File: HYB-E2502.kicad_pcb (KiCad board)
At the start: 2 copper layers, 50 x 40 mm, 23 parts, among them J1 USB4105-GF-A, U1 CH340C, U2 IM920SL, U3 NCP1117ST33T3G

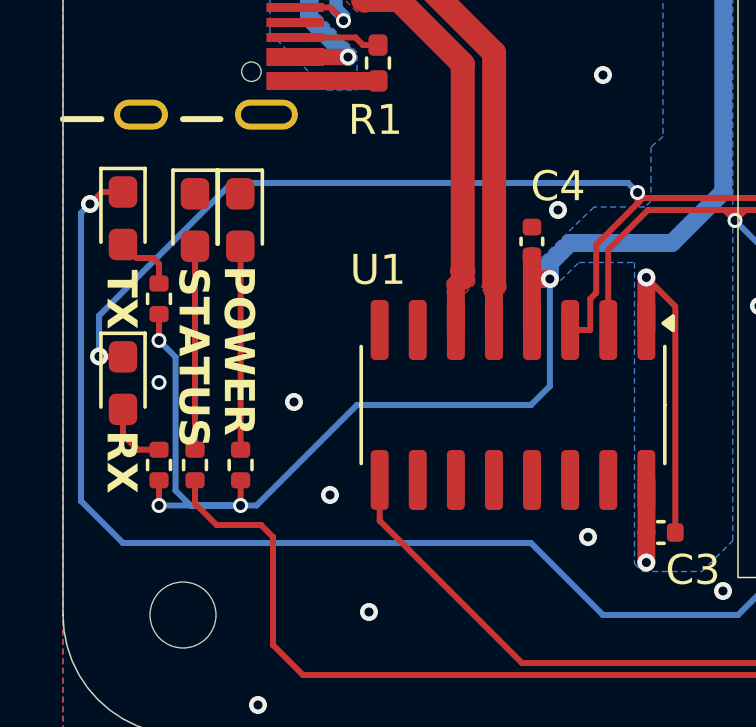
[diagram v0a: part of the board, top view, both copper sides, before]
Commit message: Edit/PCB
TX RX LEDの抵抗の位置を変更
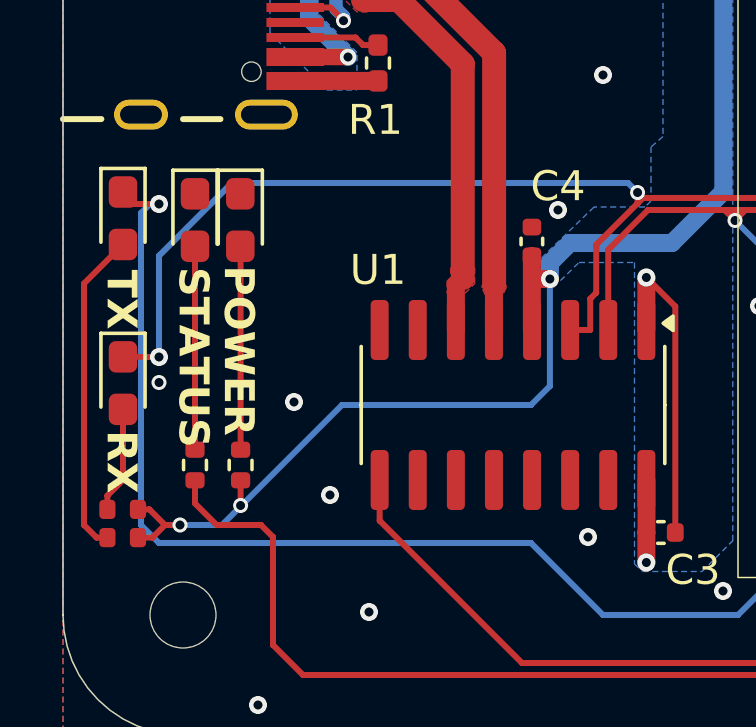
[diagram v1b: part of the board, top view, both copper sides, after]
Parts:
- moved R6 8.05 mm to (102.0, 93.4), turned to 180 degrees
- moved R5 1.91 mm to (102.0, 92.5), turned to 180 degrees
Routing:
- net Net-(D4-A): track 2.12 -> 10.8 mm
- net +3.3V: track 90.4 -> 83.3 mm, vias 6 -> 5
- net Net-(D3-A): track 2.26 -> 3.55 mm
- net Net-(D4-K): track 80.7 -> 79.6 mm
- net Net-(D3-K): track 59.7 -> 59.2 mm

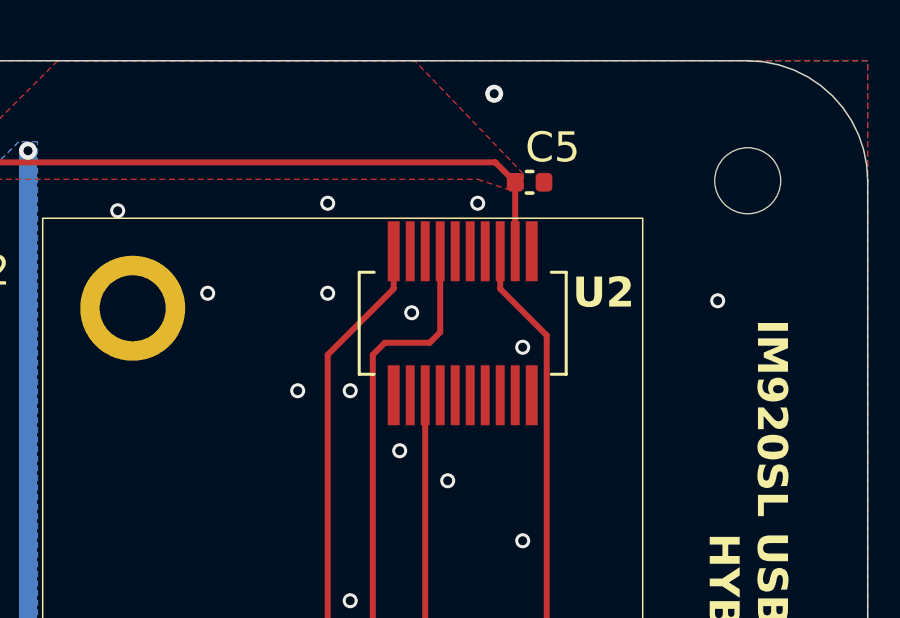
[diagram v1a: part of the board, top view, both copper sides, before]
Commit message: 配線修正
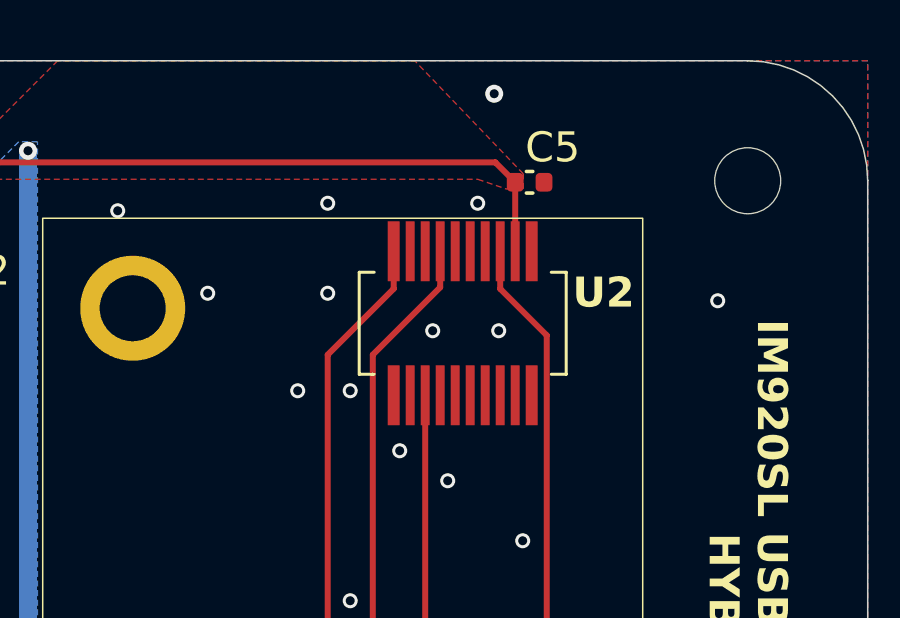
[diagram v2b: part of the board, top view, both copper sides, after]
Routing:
- net Net-(D3-K): track 59.2 -> 58.3 mm
